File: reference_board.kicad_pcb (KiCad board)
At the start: 2 copper layers, 34 x 25 mm, 31 parts, among them J1 Conn_02x05_Counter_Clockwise, U1 TMP236, U2 ADR1399, U3 LT1001

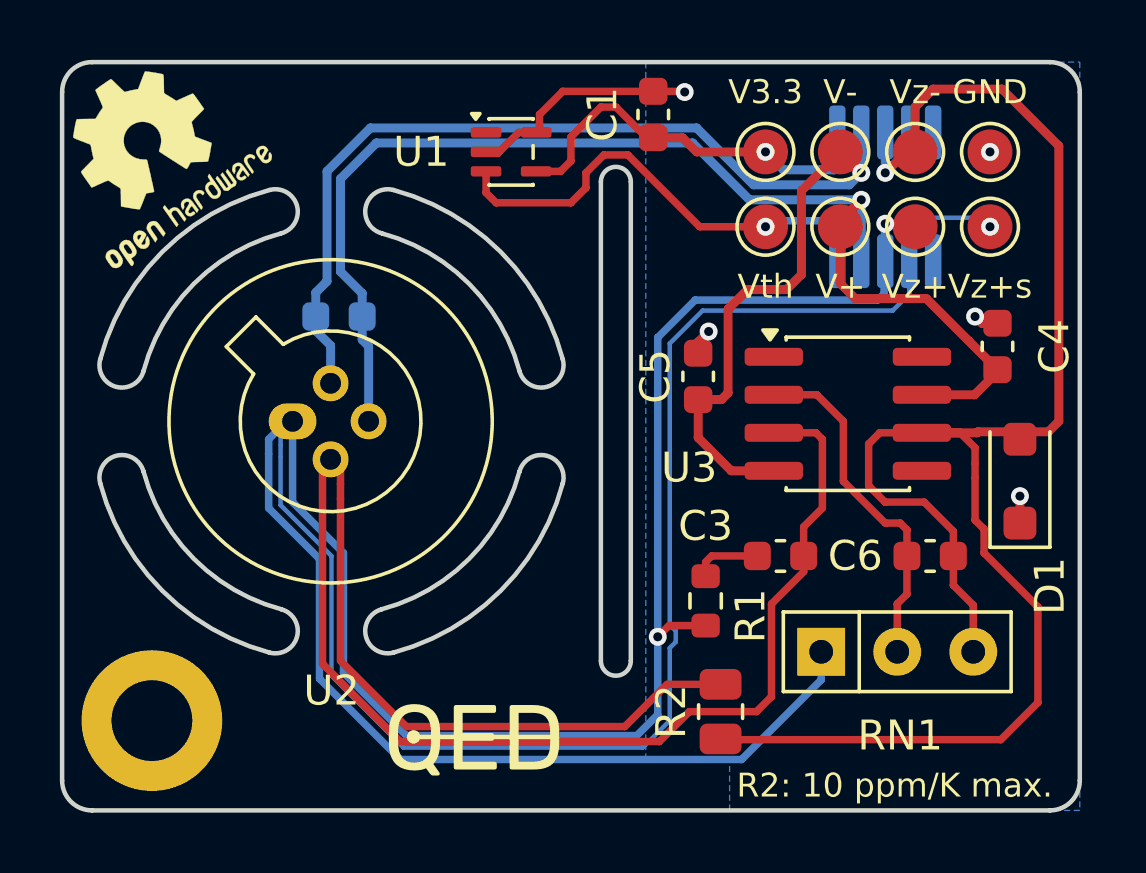
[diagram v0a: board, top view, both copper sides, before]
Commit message: Mirror the board-to-board connector to match a prototyp board.
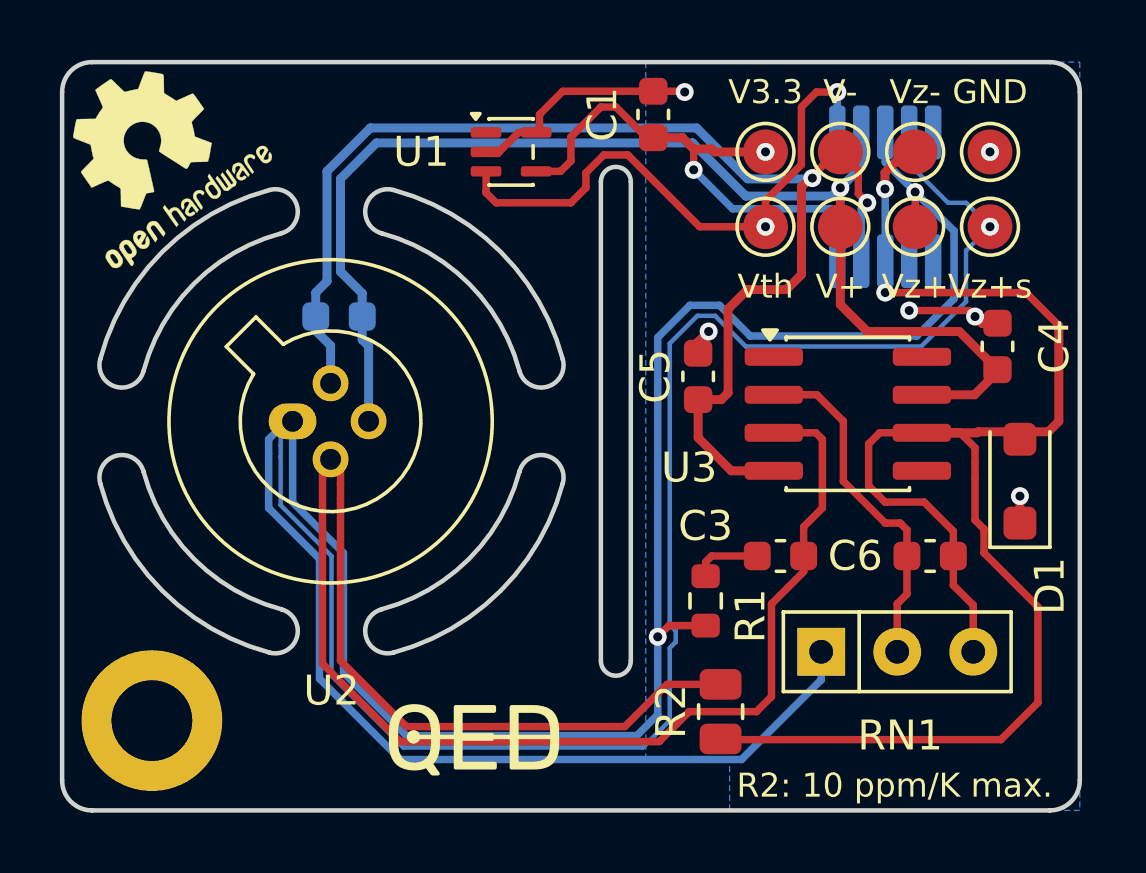
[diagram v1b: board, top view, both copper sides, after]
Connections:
- J1 pad 2: /Zener+_sense -> GND
- J1 pad 3: /Voltage Reference/V_zener+_force -> /Vout
- J1 pad 4: /Voltage Reference/V+ -> /Voltage Reference/V-
- J1 pad 5: /V_{th} -> /V3.3
- J1 pad 6: /V3.3 -> /V_{th}
- J1 pad 7: /Voltage Reference/V- -> /Voltage Reference/V+
- J1 pad 8: /Vout -> /Voltage Reference/V_zener+_force
- J1 pad 9: GND -> /Zener+_sense
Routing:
- net /Voltage Reference/V_zener+_force: track 48.2 -> 56.1 mm
- net /Zener+_sense: track 47.3 -> 52.2 mm
- net /Vout: track 27.9 -> 23.4 mm, vias 1 -> 2
- net /V3.3: track 13.4 -> 17.2 mm, vias 1 -> 2
- net /V_{th}: track 15.9 -> 19.4 mm, vias 1 -> 2
- net GND: track 11.2 -> 13.5 mm, vias 5 -> 6
- net /Voltage Reference/V-: vias 1 -> 2
